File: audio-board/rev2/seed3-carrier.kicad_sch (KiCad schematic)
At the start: 62 parts, among them J1 AudioJack2_Switch, J2 AudioJack2, J3 POWER_BOARD, J4 DISPLAY_UART, J5 SJ3-35063AG, J8 LINE_OUT, J9 SJ3-35063AG, Q1 AO3401A, Q4 2N7002, U1 TLV9064IDR, U2 TPA6132A2RTE

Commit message: Remove R5, R42, R30, R31, C27 and R36
R5 paralleled R17's bias path and only lowered the guitar input load.
R42 added nothing after the AUX path's 5k of series resistance.
HP_DETECT and PWR_BTN now use the STM32's internal pull-ups, as the
Seed3 datasheet's own switch circuits do. J5's isolated, on-board
detect switch needs no series resistor or RC either. Daisy pin 38
(3V3_D) is now unused.

C17 stays: with C9 gone it is the only ceramic at the power entry.

Co-Authored-By: Claude Opus 5.5 <noreply@anthropic.com>
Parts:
- removed C27: 100nF, Capacitor_SMD:C_1206_3216Metric_Pad1.33x1.80mm_HandSolder, symbol Device:C_Small
- removed R30, R36: 10k, Resistor_SMD:R_1206_3216Metric_Pad1.30x1.75mm_HandSolder, symbol Device:R_Small_US
- removed R31, R42: 1k, Resistor_SMD:R_1206_3216Metric_Pad1.30x1.75mm_HandSolder, symbol Device:R_Small_US
- removed R5: 10M, Resistor_SMD:R_1206_3216Metric_Pad1.30x1.75mm_HandSolder, symbol Device:R_Small_US
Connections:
- net HP_DETECT_SW is gone; now on net HP_DETECT: J5.6 (DET_NO), TP11.1
- net at C32.2, R39.2: now also U1.12 (+)
- net 3V3_D: no longer names the net of A1.38 (3V3_D)
- no-connect marks 27 -> 28

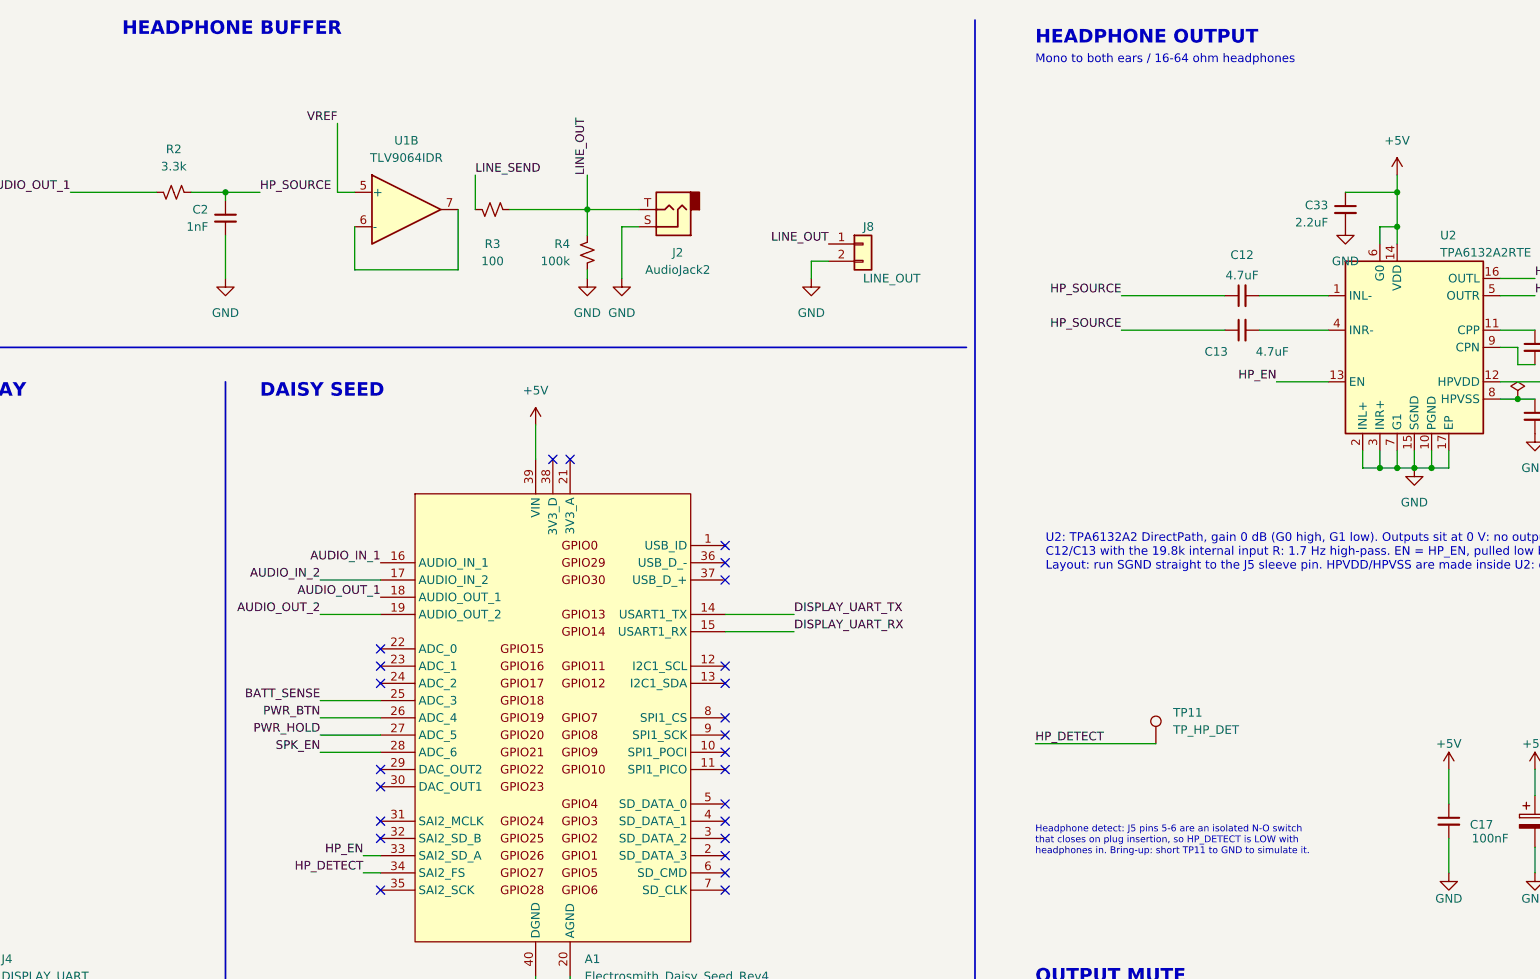
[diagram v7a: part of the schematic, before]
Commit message: Update schematic notes after the headphone buffer removal
Rename the HEADPHONE BUFFER heading to HEADPHONE FILTER and note that
U1B is parked as a VREF follower. The headphone detect note now says
HP_DETECT relies on PG9's internal pull-up, so it floats until the
firmware runs.

Co-Authored-By: Claude Opus 5.5 <noreply@anthropic.com>
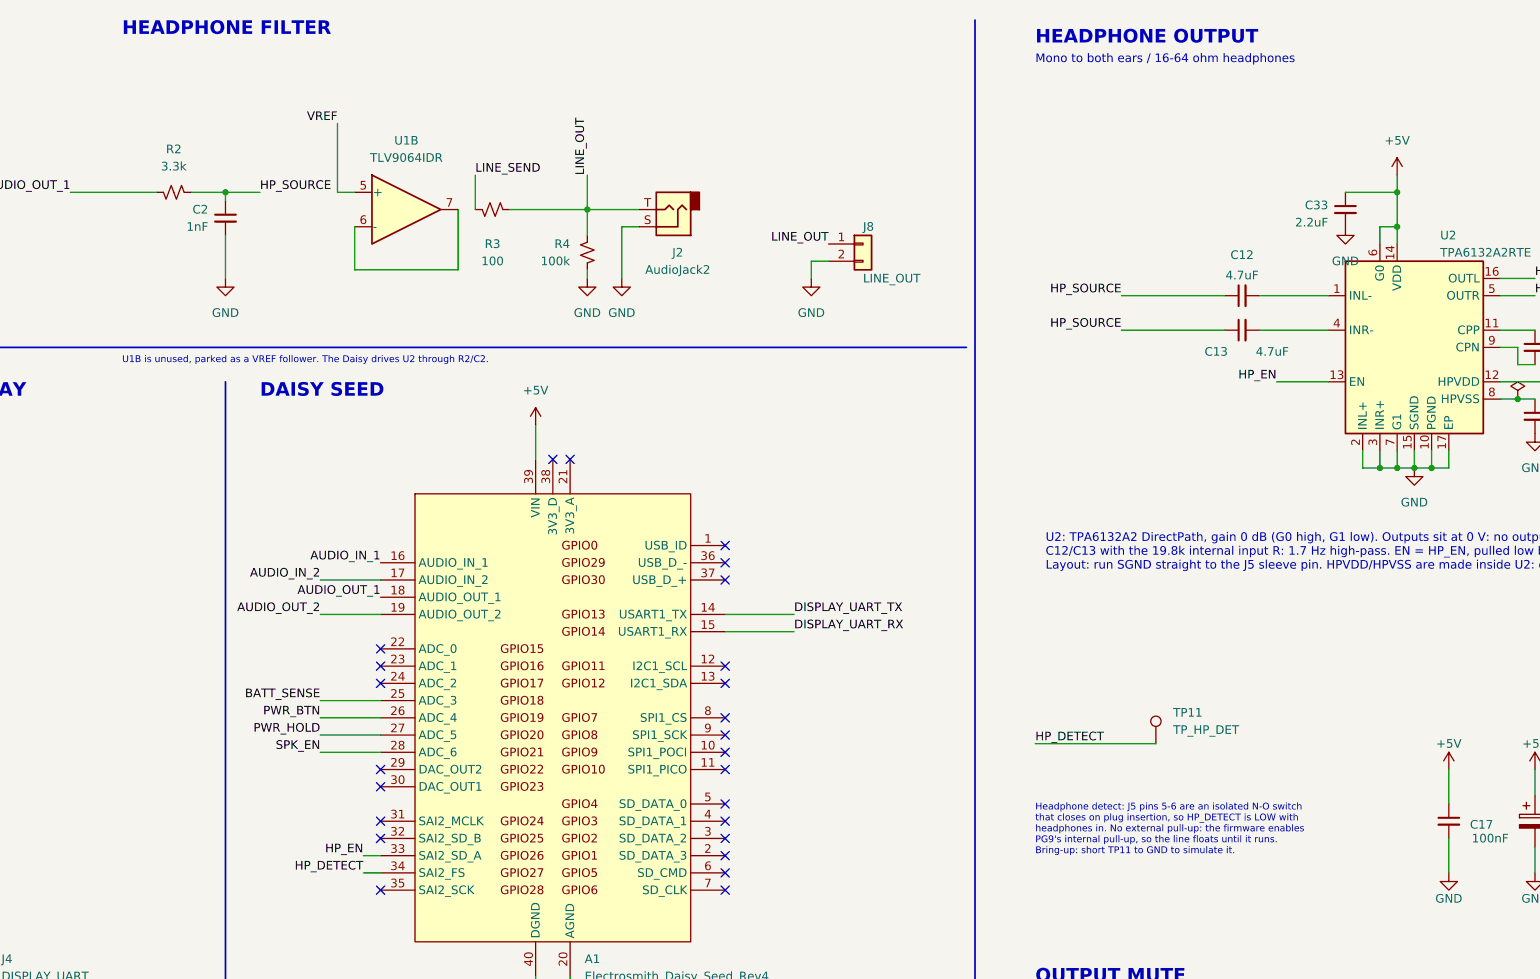
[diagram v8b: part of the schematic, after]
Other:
- note added: "HEADPHONE FILTER"
- note added: "Headphone detect: J5 pins 5-6 are an isolated N-O switch that closes on plug insertion, so HP_DETECT is LOW with headphones in. No external pull-up: the firmware enables PG9's internal pull-up, so the line floats until it runs. Bring-up: short TP11 to GND to simulate it."
- note added: "U1B is unused, parked as a VREF follower. The Daisy drives U2 through R2/C2."
- note removed: "HEADPHONE BUFFER"
- note removed: "Headphone detect: J5 pins 5-6 are an isolated N-O switch that closes on plug insertion, so HP_DETECT is LOW with headphones in. Bring-up: short TP11 to GND to simulate it."
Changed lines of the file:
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@@
 		)
 	)
-	(text "HEADPHONE BUFFER"
+	(text "HEADPHONE FILTER"
 		(exclude_from_sim no)
 		(at 154.94 17.78 0)
@@
 				(size 2 2)
 				(bold yes)
+			)
+			(justify left bottom)
+		)
+	)
+	(text "U1B is unused, parked as a VREF follower. The Daisy drives U2 through R2/C2."
+		(exclude_from_sim no)
+		(at 154.94 66.04 0)
+		(effects
+			(font
+				(size 1 1)
 			)
 			(justify left bottom)
@@
 		)
 	)
-	(text "Headphone detect: J5 pins 5-6 are an isolated N-O switch\nthat closes on plug insertion, so HP_DETECT is LOW with\nheadphones in. Bring-up: short TP11 to GND to simulate it."
+	(text "Headphone detect: J5 pins 5-6 are an isolated N-O switch\nthat closes on plug insertion, so HP_DETECT is LOW with\nheadphones in. No external pull-up: the firmware enables\nPG9's internal pull-up, so the line floats until it runs.\nBring-up: short TP11 to GND to simulate it."
 		(exclude_from_sim no)
 		(at 289.56 138.43 0)
